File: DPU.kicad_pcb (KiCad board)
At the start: 2 copper layers, 31.8 x 36.8 mm, 10 parts, among them U1 74LS04, Y1 8Mhz

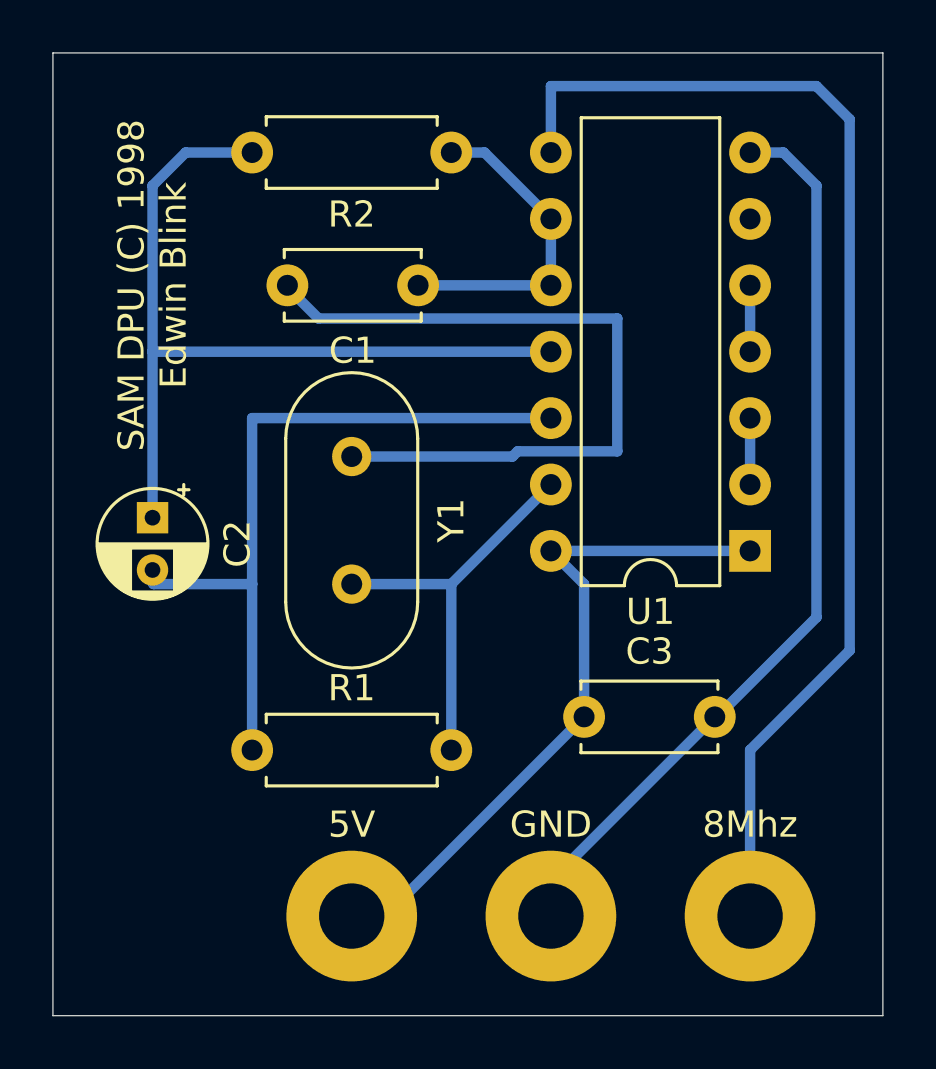
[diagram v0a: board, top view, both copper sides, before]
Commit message: Updated PCB (Kicad 8.0)
Smaller PCB for easier mounting inside case and reduced wire holes to sensible size.
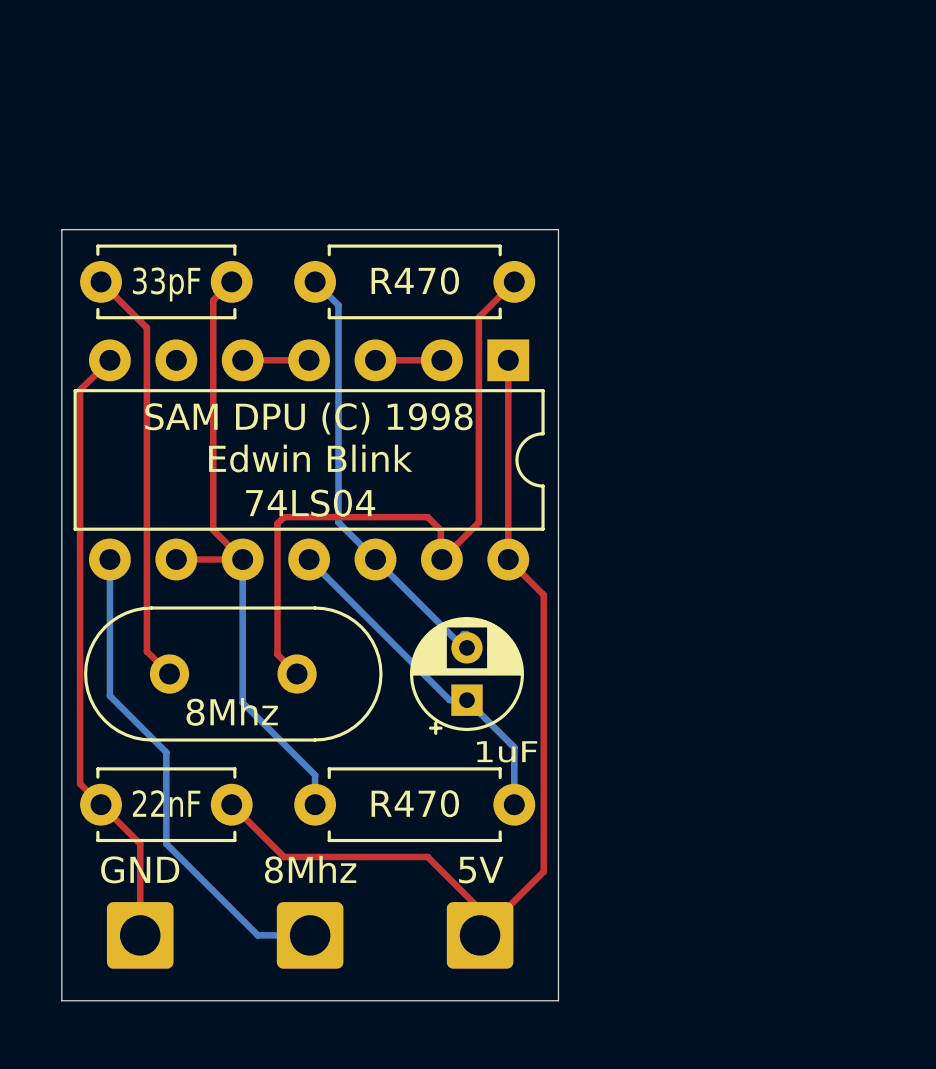
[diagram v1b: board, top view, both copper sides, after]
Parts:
- 5V, 8Mhz, GND: footprint MountingHole:MountingHole_2.5mm_Pad -> Connector_Wire:SolderWire-0.75sqmm_1x01_D1.25mm_OD2.3mm
- moved R2 25.5 mm to (147.2, 107.5), turned to 0 degrees
- moved R1 18.1 mm to (147.2, 87.5)
- moved 8Mhz 16.8 mm to (147.0, 112.5)
- moved GND 15.7 mm to (140.5, 112.5)
- moved C2 13.9 mm to (153.0, 103.5), turned to 90 degrees
- moved C3 13.9 mm to (144.0, 107.5), turned to 180 degrees
- moved U1 11.8 mm to (154.6, 90.5), turned to -90 degrees
- moved C1 7.13 mm to (144.0, 87.5)
- moved 5V 4.97 mm to (153.5, 112.5)
- moved Y1 4.03 mm to (146.5, 102.5), turned to 180 degrees
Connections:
- U1 pad 6: Net-(U1-Pad6) -> unconnected-(U1-Pad6)
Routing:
- net Net-(8Mhz1-Pad1): track 47.8 -> 18.7 mm
- net Net-(C2-Pad1): track 32.3 -> 13.2 mm
- net Net-(C1-Pad2): track 28.6 -> 16.1 mm
- net Net-(C1-Pad1): track 12.5 -> 24.4 mm
- net Net-(U1G-GND): track 35.4 -> 23.5 mm
- net Net-(C2-Pad2): track 28.0 -> 16.6 mm
- net Net-(R1-Pad2): track 15.5 -> 26.2 mm
- net Net-(U1G-VCC): track 26.5 -> 35.7 mm
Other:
- board size 31.8 x 36.8 mm -> 19 x 29.5 mm
- net class Default removed
- board text added: "PCB 2024 Dan Dooré"
- board text removed: "PCB 2021 Dan Dooré"
